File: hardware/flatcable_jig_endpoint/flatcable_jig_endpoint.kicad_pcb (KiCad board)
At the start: 2 copper layers, 40 x 22 mm, 17 parts, among them J1 Coax, J3 Conn_01x03, J4 Conn_01x03, J5 Conn_02x05_Odd_Even

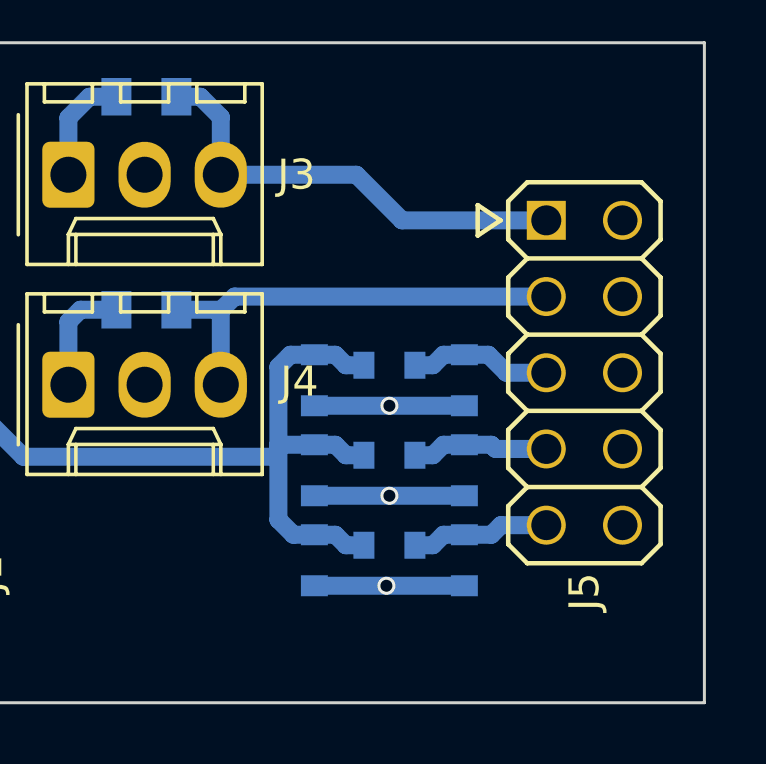
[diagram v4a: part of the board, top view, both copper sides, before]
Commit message: added jumperable grounds
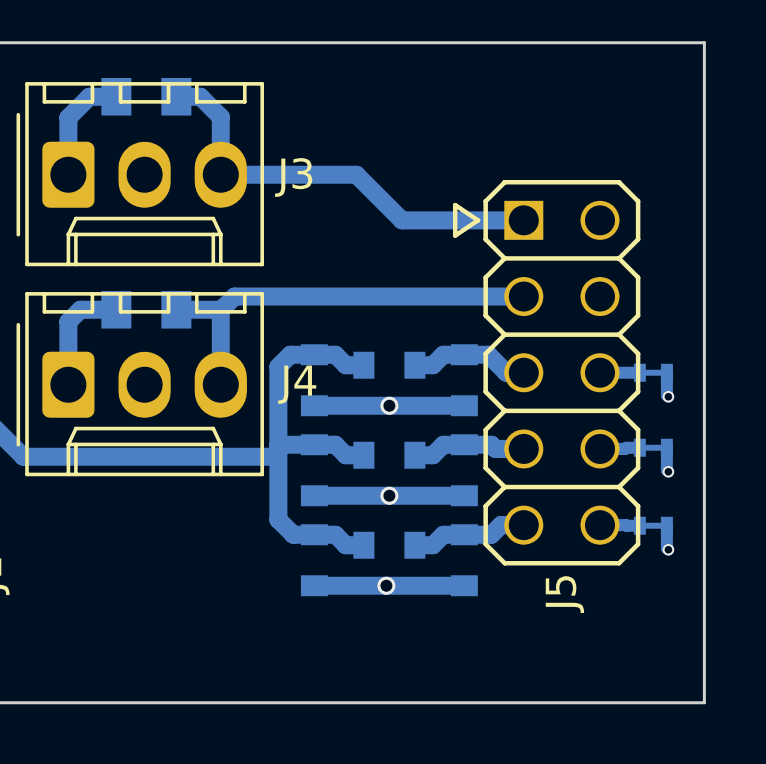
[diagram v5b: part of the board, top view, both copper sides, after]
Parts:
- added SJ1: SolderJumper_2way_1conn, SquantorSpecial:solder_jumper_2way_conn, B.Cu at (138.3, 111.0)
- added SJ2: SolderJumper_2way_1conn, SquantorSpecial:solder_jumper_2way_conn, B.Cu at (138.3, 113.5)
- added SJ3: SolderJumper_2way_1conn, SquantorSpecial:solder_jumper_2way_conn, B.Cu at (138.3, 116.1)
- moved J5 0.75 mm to (135.2, 111.0)
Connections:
- J3 pad 2: Net-(J3-Pad2) -> (no net)
- J4 pad 2: Net-(J4-Pad2) -> (no net)
- J5 pad 10: GND -> Net-(J5-Pad10)
- J5 pad 6: GND -> Net-(J5-Pad6)
- J5 pad 8: GND -> Net-(J5-Pad8)
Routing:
- net GND: track 22.7 -> 25.1 mm, vias 3 -> 6
- net Net-(J5-Pad8): track 0.00 -> 1.35 mm
- net Net-(J5-Pad10): track 0.00 -> 1.34 mm
- net Net-(J5-Pad6): track 0.00 -> 1.33 mm
- net /SIGNAL_1: track 4.58 -> 3.83 mm
- net /SIGNAL_2: track 4.66 -> 3.91 mm
- net /SIGNAL_0: track 4.77 -> 4.02 mm
- net /POWER_1: track 15.0 -> 14.3 mm
- net /POWER_0: track 15.2 -> 14.4 mm

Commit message: updated versionnumbers, no real changes actually
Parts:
- N2: value 20181216 -> 20190121
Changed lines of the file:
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@@
   )
   (setup
-    (last_trace_width 0.4)
+    (last_trace_width 0.1524)
     (user_trace_width 0.1524)
     (user_trace_width 0.2)
@@
       (effects (font (size 1 1) (thickness 0.15)))
     )
-    (fp_text value 20181216 (at -0.4 -0.1 270) (layer B.SilkS)
+    (fp_text value 20190121 (at -0.4 -0.1 270) (layer B.SilkS)
       (effects (font (size 1 1) (thickness 0.15)) (justify mirror))
     )
